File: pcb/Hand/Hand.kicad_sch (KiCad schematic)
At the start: 38 parts, among them J1 Conn_01x08_IMU_1, J10 Conn_01x03_HALL_7, J11 Conn_01x03_HALL_8, J12 Conn_01x03_HALL_9, J13 Conn_01x03_HALL_10, J14 Conn_01x03_HALL_11, J15 Conn_01x03_HALL_12, J16 Conn_01x03_HALL_13, J17 Conn_01x03_HALL_14, J18 Conn_01x03_HALL_15, J19 Conn_01x05_HAPTIC_1, J2 Conn_01x03_HALL_0, J20 Conn_01x05_HAPTIC_2, J21 Conn_01x05_HAPTIC_3, J22 Conn_01x05_HAPTIC_4, J23 Conn_01x03_FEEDBACK_0, J24 Conn_01x03_FEEDBACK_1, J25 Conn_01x03_FEEDBACK_2, J26 Conn_01x03_FEEDBACK_3, J27 Conn_01x03_FEEDBACK_4, J28 Conn_01x03_SPOOLPOT_1, J29 Conn_01x03_SPOOLPOT_2, J3 Conn_01x05_HAPTIC_0, J30 Conn_01x03_SPOOLPOT_3, J31 Conn_01x03_SPOOLPOT_0, J32 Conn_01x03_SPOOLPOT_4, J33 Conn_01x16_Ribbon_Bottom, J34 Conn_01x16_Ribbon_Top, J4 Conn_01x03_HALL_1, J5 Conn_01x03_HALL_2, J6 Conn_01x03_HALL_3, J7 Conn_01x03_HALL_4, J8 Conn_01x03_HALL_5, J9 Conn_01x03_HALL_6, U1 CD74HC4067M96, U3 TCA9548A

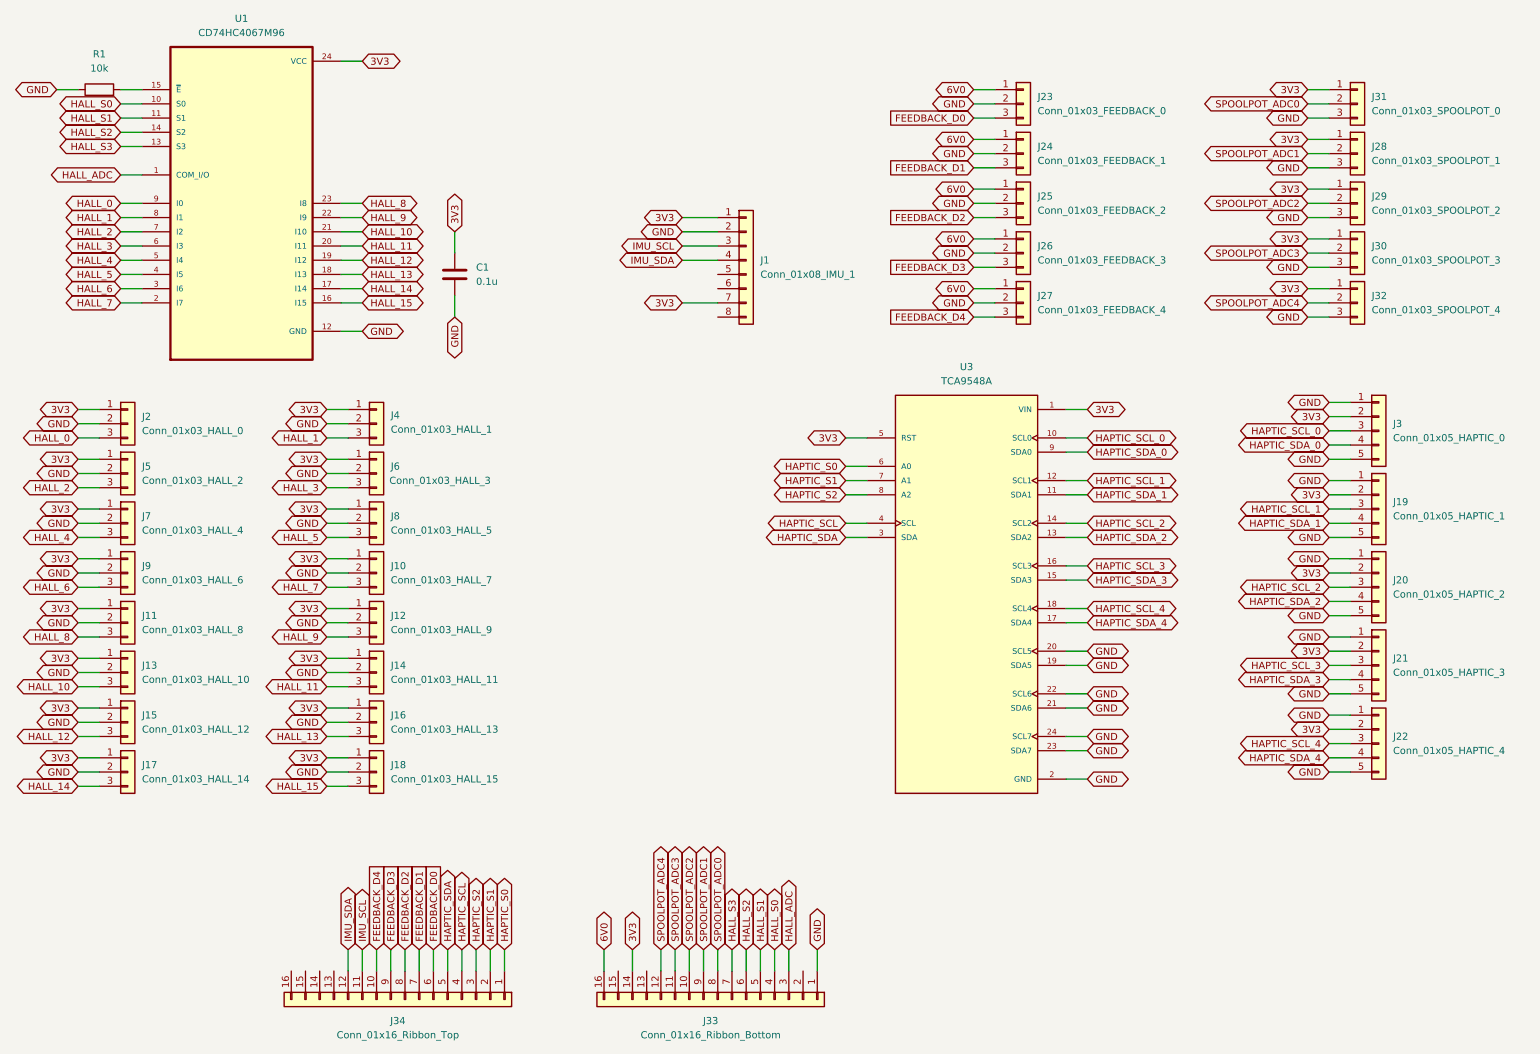
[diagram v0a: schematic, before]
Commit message: forward annotated schms to pcbs, added gnd and pwr planes, begun part placement
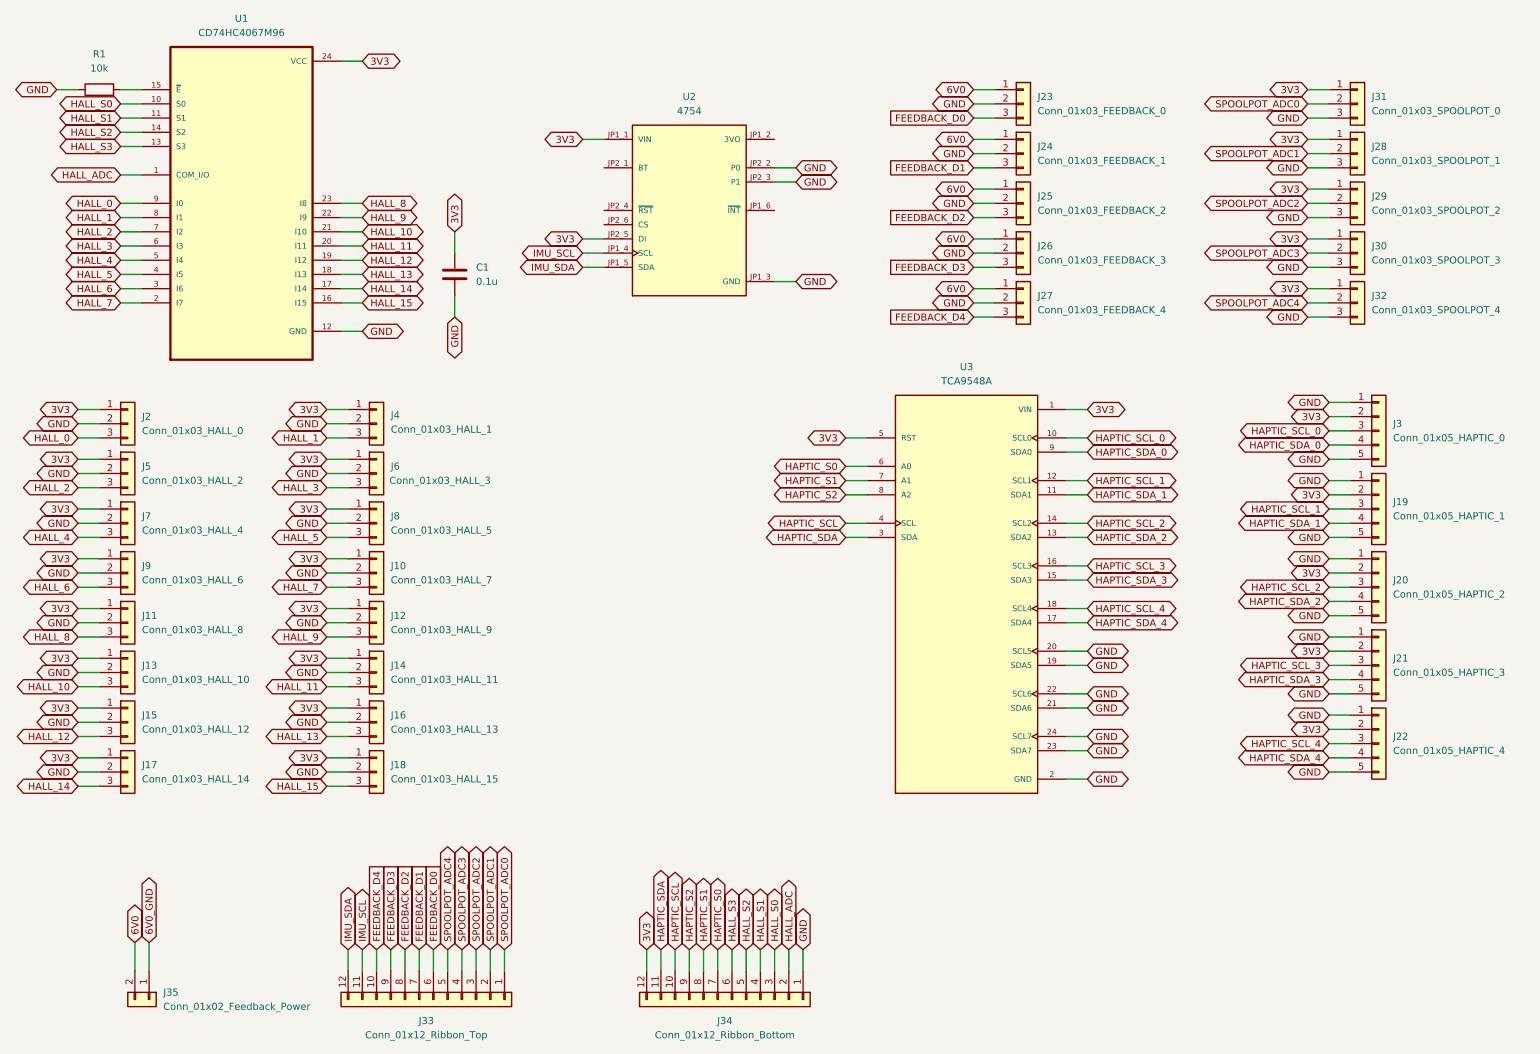
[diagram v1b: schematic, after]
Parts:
- removed J1: Conn_01x08_IMU_1, symbol Connector_Generic:Conn_01x08
- removed J33: Conn_01x16_Ribbon_Bottom, symbol Connector_Generic:Conn_01x16
- removed J34: Conn_01x16_Ribbon_Top, symbol Connector_Generic:Conn_01x16
- added J33: Conn_01x12_Ribbon_Top, 0522071233:0522071233, symbol Connector_Generic:Conn_01x12
- added J34: Conn_01x12_Ribbon_Bottom, 0522071233:0522071233, symbol Connector_Generic:Conn_01x12
- added J35: Conn_01x02_Feedback_Power, Connector_PinHeader_2.54mm:PinHeader_1x02_P2.54mm_Vertical_SMD_Pin1Left, symbol Connector_Generic:Conn_01x02
- added U2: 4754, BNO085:MODULE_4754, symbol BNO085:4754
- C1: footprint (none) -> Capacitor_THT:CP_Radial_D5.0mm_P2.50mm
- J10, J11, J12, J13, J14, J15, J16, J17, J18, J2, J23, J24, J25, J26, J27, J28, J29, J30, J31, J32, J4, J5, J6, J7, J8, J9: footprint (none) -> SM03B-SRSS-TB:JST_SM03B-SRSS-TB_LF__SN_
- J19, J20, J21, J22, J3: footprint (none) -> SM05B-SRSS-TB:JST_SM05B-SRSS-TB_LF__SN_
- R1: footprint (none) -> Resistor_THT:R_Axial_DIN0207_L6.3mm_D2.5mm_P10.16mm_Horizontal
- U3: footprint 2717:MODULE_2717 -> TCA9548A:MODULE_2717
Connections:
- net 3V3: now also J34.12 (Pin_12), U2.JP1_1 (VIN), U2.JP2_5 (DI)
- net 6V0: now also J35.2 (Pin_2)
- net FEEDBACK_D0: now also J33.6 (Pin_6)
- net FEEDBACK_D1: now also J33.7 (Pin_7)
- net FEEDBACK_D2: now also J33.8 (Pin_8)
- net FEEDBACK_D3: now also J33.9 (Pin_9)
- net FEEDBACK_D4: now also J33.10 (Pin_10)
- net GND: now also J34.1 (Pin_1), U2.JP1_3 (GND), U2.JP2_2 (P0), U2.JP2_3 (P1)
- net HALL_ADC: now also J34.2 (Pin_2)
- net HALL_S0: now also J34.3 (Pin_3)
- net HALL_S1: now also J34.4 (Pin_4)
- net HALL_S2: now also J34.5 (Pin_5)
- net HALL_S3: now also J34.6 (Pin_6)
- net HAPTIC_S0: now also J34.7 (Pin_7)
- net HAPTIC_S1: now also J34.8 (Pin_8)
- net HAPTIC_S2: now also J34.9 (Pin_9)
- net HAPTIC_SCL: now also J34.10 (Pin_10)
- net HAPTIC_SDA: now also J34.11 (Pin_11)
- net IMU_SCL: now also J33.11 (Pin_11), U2.JP1_4 (SCL)
- net IMU_SDA: now also J33.12 (Pin_12), U2.JP1_5 (SDA)
- net SPOOLPOT_ADC0: now also J33.1 (Pin_1)
- net SPOOLPOT_ADC1: now also J33.2 (Pin_2)
- net SPOOLPOT_ADC2: now also J33.3 (Pin_3)
- net SPOOLPOT_ADC3: now also J33.4 (Pin_4)
- net SPOOLPOT_ADC4: now also J33.5 (Pin_5)
- new net 6V0_GND: J35.1 (Pin_1)

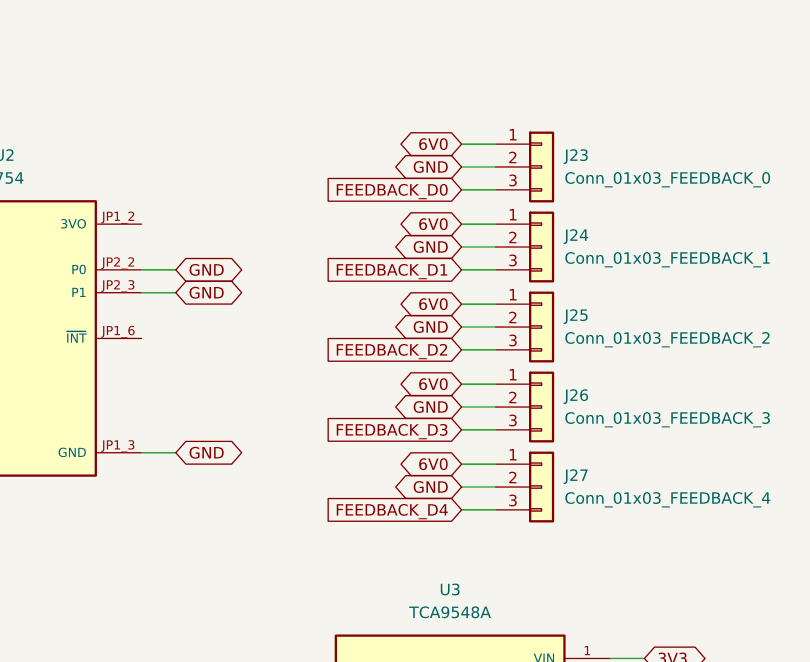
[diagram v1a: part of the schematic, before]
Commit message: completed tentative part layout
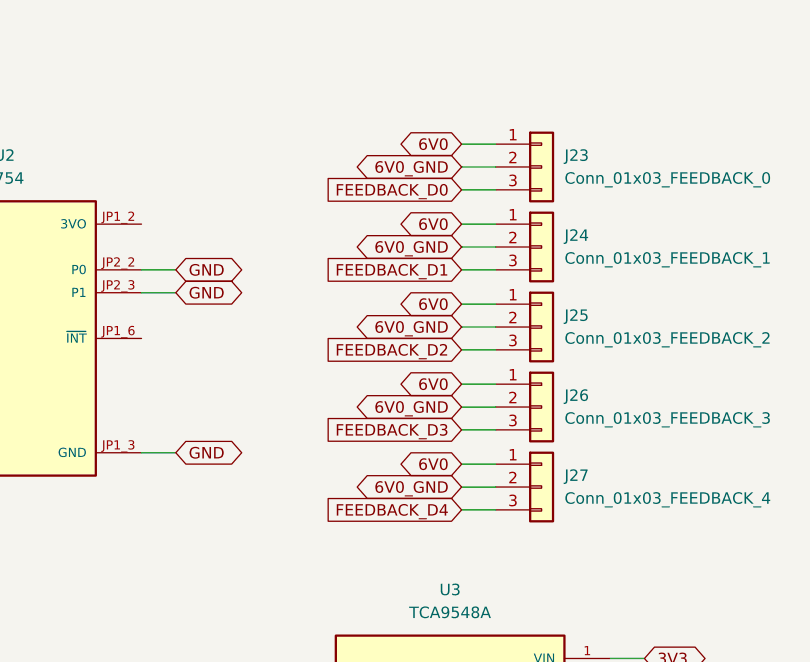
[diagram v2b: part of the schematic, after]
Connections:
- net 6V0_GND: now also J23.2 (Pin_2), J24.2 (Pin_2), J25.2 (Pin_2), J26.2 (Pin_2), J27.2 (Pin_2)
- net GND: no longer J23.2 (Pin_2), J24.2 (Pin_2), J25.2 (Pin_2), J26.2 (Pin_2), J27.2 (Pin_2)
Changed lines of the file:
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@@
 	(global_label "GND"
 		(shape bidirectional)
-		(at 186.69 38.1 180)
-		(fields_autoplaced yes)
-		(effects
-			(font
-				(size 1.27 1.27)
-			)
-			(justify right)
-		)
-		(property "Intersheetrefs" "${INTERSHEET_REFS}"
-			(at 178.723 38.1 0)
-			(effects
-				(font
-					(size 1.27 1.27)
-				)
-				(justify right)
-				(hide yes)
-			)
-		)
-	)
-	(global_label "GND"
-		(shape bidirectional)
 		(at 22.86 26.67 180)
 		(fields_autoplaced yes)
@@
 		)
 	)
-	(global_label "GND"
-		(shape bidirectional)
-		(at 186.69 64.77 180)
-		(fields_autoplaced yes)
-		(effects
-			(font
-				(size 1.27 1.27)
-			)
-			(justify right)
-		)
-		(property "Intersheetrefs" "${INTERSHEET_REFS}"
-			(at 178.723 64.77 0)
-			(effects
-				(font
-					(size 1.27 1.27)
-				)
-				(justify right)
-				(hide yes)
-			)
-		)
-	)
 	(global_label "HALL_8"
 		(shape bidirectional)
@@
 	(global_label "GND"
 		(shape bidirectional)
-		(at 186.69 29.21 180)
-		(fields_autoplaced yes)
-		(effects
-			(font
-				(size 1.27 1.27)
-			)
-			(justify right)
-		)
-		(property "Intersheetrefs" "${INTERSHEET_REFS}"
-			(at 178.723 29.21 0)
-			(effects
-				(font
-					(size 1.27 1.27)
-				)
-				(justify right)
-				(hide yes)
-			)
-		)
-	)
-	(global_label "GND"
-		(shape bidirectional)
 		(at 207.01 129.54 0)
 		(fields_autoplaced yes)
@@
 		)
 	)
+	(global_label "6V0_GND"
+		(shape bidirectional)
+		(at 186.69 38.1 180)
+		(fields_autoplaced yes)
+		(effects
+			(font
+				(size 1.27 1.27)
+			)
+			(justify right)
+		)
+		(property "Intersheetrefs" "${INTERSHEET_REFS}"
+			(at 174.2478 38.1 0)
+			(effects
+				(font
+					(size 1.27 1.27)
+				)
+				(justify right)
+				(hide yes)
+			)
+		)
+	)
 	(global_label "3V3"
 		(shape bidirectional)
@@
 		)
 	)
+	(global_label "6V0_GND"
+		(shape bidirectional)
+		(at 186.69 46.99 180)
+		(fields_autoplaced yes)
+		(effects
+			(font
+				(size 1.27 1.27)
+			)
+			(justify right)
+		)
+		(property "Intersheetrefs" "${INTERSHEET_REFS}"
+			(at 174.2478 46.99 0)
+			(effects
+				(font
+					(size 1.27 1.27)
+				)
+				(justify right)
+				(hide yes)
+			)
+		)
+	)
 	(global_label "GND"
 		(shape bidirectional)
@@
 		)
 	)
+	(global_label "6V0_GND"
+		(shape bidirectional)
+		(at 186.69 55.88 180)
+		(fields_autoplaced yes)
+		(effects
+			(font
+				(size 1.27 1.27)
+			)
+			(justify right)
+		)
+		(property "Intersheetrefs" "${INTERSHEET_REFS}"
+			(at 174.2478 55.88 0)
+			(effects
+				(font
+					(size 1.27 1.27)
+				)
+				(justify right)
+				(hide yes)
+			)
+		)
+	)
 	(global_label "6V0"
 		(shape bidirectional)
@@
 		)
 	)
-	(global_label "GND"
+	(global_label "HAPTIC_SDA_4"
 		(shape bidirectional)
-		(at 186.69 55.88 180)
+		(at 250.19 146.05 180)
 		(fields_autoplaced yes)
 		(effects
@@
 		)
 		(property "Intersheetrefs" "${INTERSHEET_REFS}"
-			(at 178.723 55.88 0)
+			(at 232.8492 146.05 0)
 			(effects
 				(font
@@
 		)
 	)
-	(global_label "HAPTIC_SDA_4"
+	(global_label "6V0_GND"
 		(shape bidirectional)
-		(at 250.19 146.05 180)
+		(at 186.69 64.77 180)
 		(fields_autoplaced yes)
 		(effects
@@
 		)
 		(property "Intersheetrefs" "${INTERSHEET_REFS}"
-			(at 232.8492 146.05 0)
+			(at 174.2478 64.77 0)
 			(effects
 				(font
@@
 		)
 	)
+	(global_label "6V0_GND"
+		(shape bidirectional)
+		(at 186.69 29.21 180)
+		(fields_autoplaced yes)
+		(effects
+			(font
+				(size 1.27 1.27)
+			)
+			(justify right)
+		)
+		(property "Intersheetrefs" "${INTERSHEET_REFS}"
+			(at 174.2478 29.21 0)
+			(effects
+				(font
+					(size 1.27 1.27)
+				)
+				(justify right)
+				(hide yes)
+			)
+		)
+	)
 	(global_label "HALL_14"
 		(shape bidirectional)
@@
 				(hide yes)
 			)
-		)
-	)
-	(global_label "GND"
-		(shape bidirectional)
-		(at 186.69 46.99 180)
-		(fields_autoplaced yes)
-		(effects
-			(font
-				(size 1.27 1.27)
-			)
-			(justify right)
-		)
-		(property "Intersheetrefs" "${INTERSHEET_REFS}"
-			(at 178.723 46.99 0)
-			(effects
-				(font
-					(size 1.27 1.27)
-				)
-				(justify right)
-				(hide yes)
-			)
